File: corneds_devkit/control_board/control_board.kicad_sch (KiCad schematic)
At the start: 0 parts

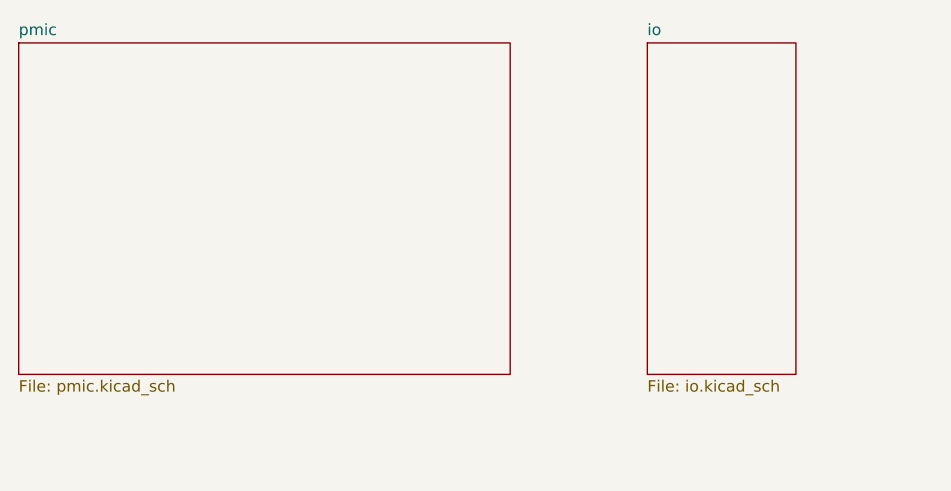
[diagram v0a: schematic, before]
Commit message: removed nucleo board because we're not using that mcu anymore and started control board
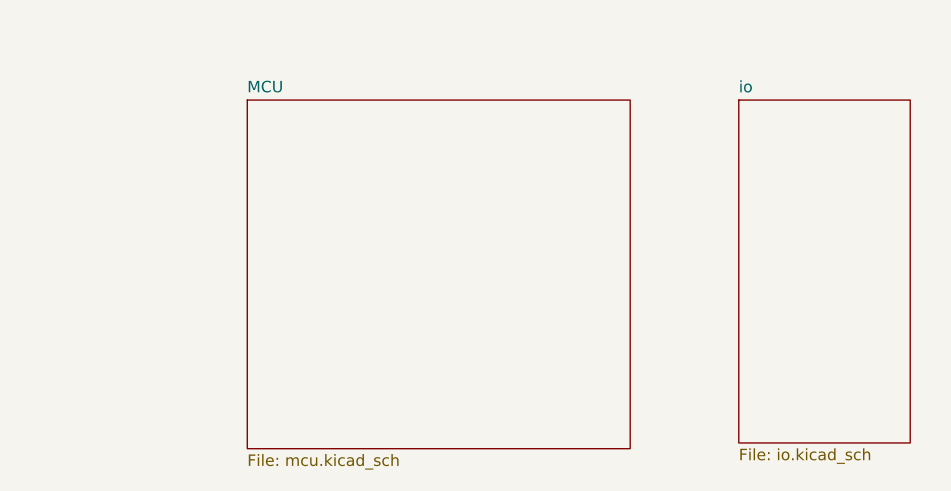
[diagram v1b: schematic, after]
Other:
- removed sheet pmic
- added sheet MCU (mcu.kicad_sch)
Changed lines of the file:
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@@
 	(paper "A4")
 	(sheet
-		(at 39.37 33.02)
-		(size 54.61 36.83)
+		(at 64.77 39.37)
+		(size 42.545 38.735)
 		(fields_autoplaced yes)
 		(stroke
@@
 			(color 0 0 0 0.0000)
 		)
-		(property "Sheetname" "pmic"
-			(at 39.37 32.3084 0)
+		(property "Sheetname" "MCU"
+			(at 64.77 38.6584 0)
 			(effects
 				(font
@@
 			)
 		)
-		(property "Sheetfile" "pmic.kicad_sch"
-			(at 39.37 70.4346 0)
+		(property "Sheetfile" "mcu.kicad_sch"
+			(at 64.77 78.6896 0)
 			(effects
 				(font
@@
 		)
 		(instances
-			(project "power_board"
-				(path "/e1d68063-f971-488f-82e1-71c760b8d683"
+			(project "control_board"
+				(path "/765a8bd0-01ed-4bd6-922e-680c17625fb8"
 					(page "2")
 				)
@@
 	)
 	(sheet
-		(at 109.22 33.02)
-		(size 16.51 36.83)
+		(at 119.38 39.37)
+		(size 19.05 38.1)
 		(fields_autoplaced yes)
 		(stroke
@@
 		)
 		(property "Sheetname" "io"
-			(at 109.22 32.3084 0)
+			(at 119.38 38.6584 0)
 			(effects
 				(font
@@
 		)
 		(property "Sheetfile" "io.kicad_sch"
-			(at 109.22 70.4346 0)
+			(at 119.38 78.0546 0)
 			(effects
 				(font
@@
 		)
 		(instances
-			(project "power_board"
-				(path "/e1d68063-f971-488f-82e1-71c760b8d683"
+			(project "control_board"
+				(path "/765a8bd0-01ed-4bd6-922e-680c17625fb8"
 					(page "3")
 				)
